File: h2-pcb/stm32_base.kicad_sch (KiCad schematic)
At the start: 42 parts, among them J1 Network Connector, J2 STDC14, SW1 SW_Push, U1 LD39050PU33R, U2 STM32G474RBT6, U3 SN65HVD230, Y1 8MHz

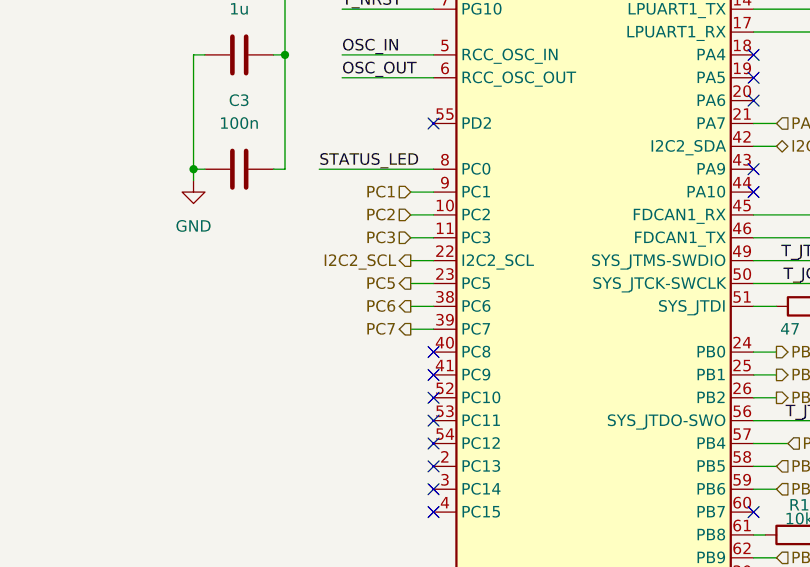
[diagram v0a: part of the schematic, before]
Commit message: Update sur le routage, silkscreen, jlcpcb parts #
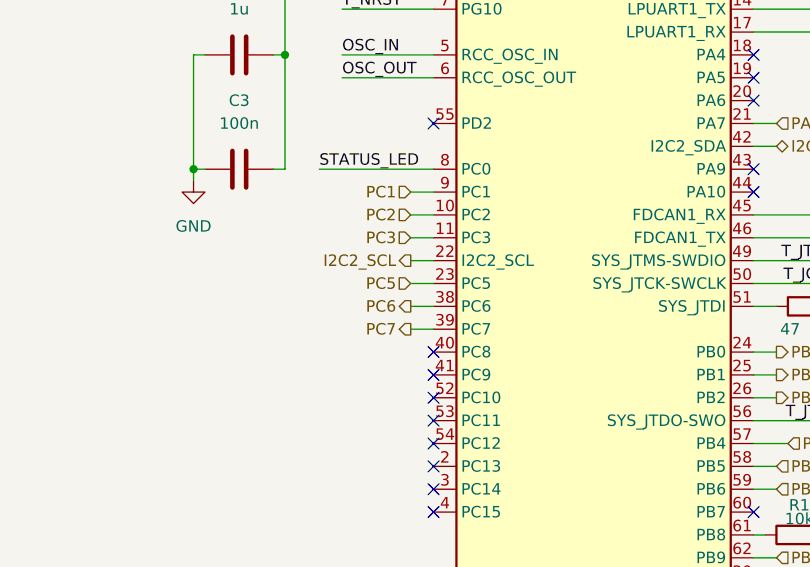
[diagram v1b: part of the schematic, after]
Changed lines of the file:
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@@
 	)
 	(hierarchical_label "PC5"
-		(shape output)
+		(shape input)
 		(at 60.96 130.81 180)
 		(effects

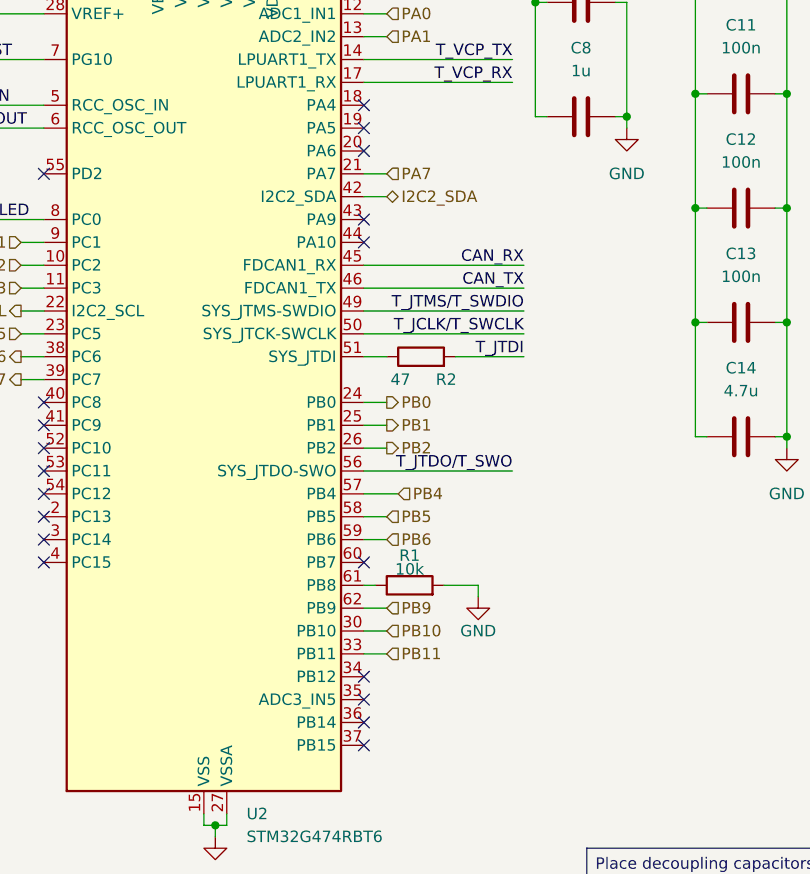
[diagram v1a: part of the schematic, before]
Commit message: h2-pcb: rename PA7 label to PB13
The pin function for PB13 on the MCU was modified, but the hierarchical
label wasn't updated. The one that used to be called "PA7" was renamed
to "PB13" and connected to that pin.

Also updated the routing to refelct these changes.
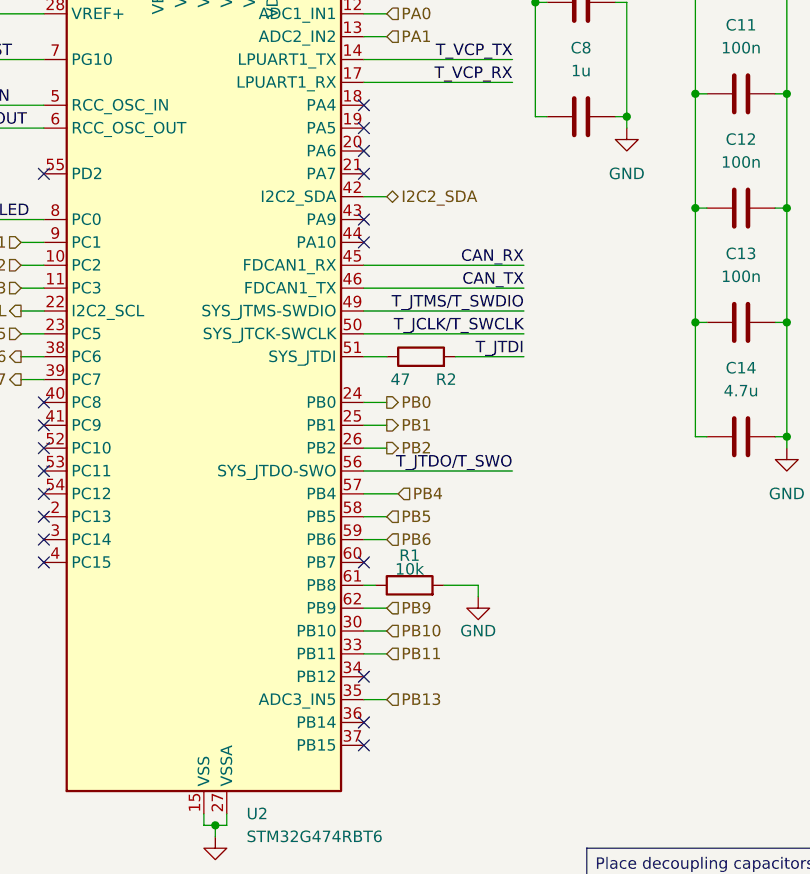
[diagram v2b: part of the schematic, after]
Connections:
- net PB13: now reaches U2.35 (PB13)
- net PA7: no longer names the net of U2.21 (PA7)
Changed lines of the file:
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@@
-	)
-	(no_connect
-		(at 99.06 171.45)
 	)
 	(no_connect
@@
 	)
 	(no_connect
+		(at 99.06 113.03)
+	)
+	(no_connect
 		(at 99.06 176.53)
 	)
@@
 	(wire
 		(pts
+			(xy 99.06 171.45) (xy 101.6 171.45)
+		)
+		(stroke
+			(width 0)
+			(type default)
+		)
+	)
+	(wire
+		(pts
 			(xy 144.78 104.14) (xy 146.05 104.14)
 		)
@@
 		(pts
 			(xy 135.89 116.84) (xy 135.89 129.54)
-		)
-		(stroke
-			(width 0)
-			(type default)
-		)
-	)
-	(wire
-		(pts
-			(xy 99.06 113.03) (xy 101.6 113.03)
 		)
 		(stroke
@@
 		)
 	)
-	(hierarchical_label "PA7"
-		(shape input)
-		(at 101.6 113.03 0)
-		(effects
-			(font
-				(size 1.27 1.27)
-			)
-			(justify left)
-		)
-	)
 	(hierarchical_label "PC7"
 		(shape output)
@@
 		(effects
 			(font
+				(size 1.27 1.27)
+			)
+			(justify left)
+		)
+	)
+	(hierarchical_label "PB13"
+		(shape input)
+		(at 101.6 171.45 0)
+		(effects
+			(font

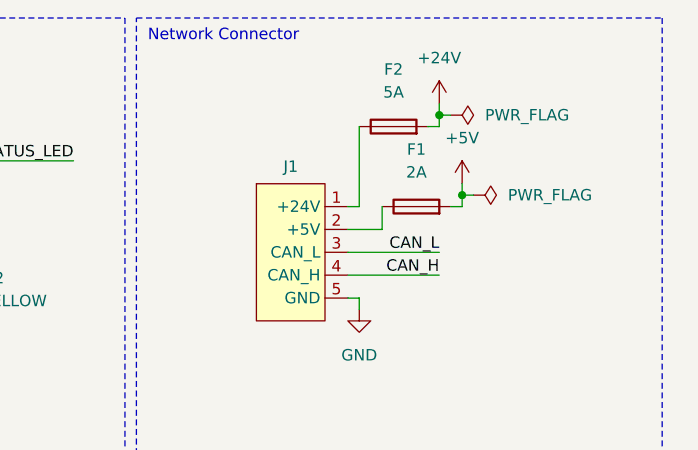
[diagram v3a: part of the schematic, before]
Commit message: h2-pcb: implement review comments
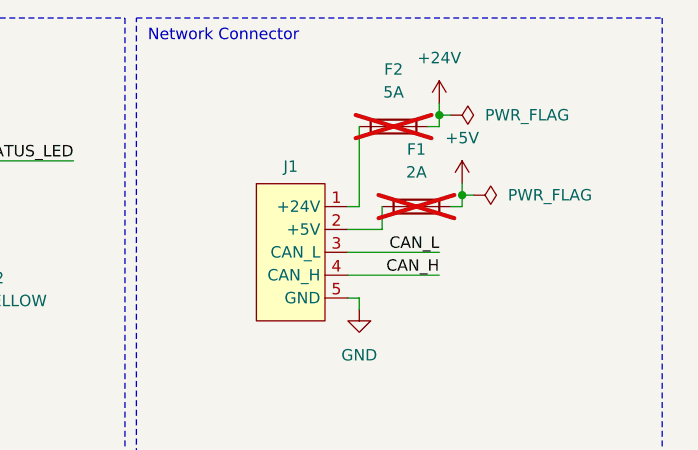
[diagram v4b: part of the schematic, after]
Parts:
- F1, F2: now not fitted
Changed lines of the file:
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@@
 		(in_bom yes)
 		(on_board yes)
-		(dnp no)
+		(dnp yes)
 		(fields_autoplaced yes)
 		(property "Reference" "F2"
@@
 		(in_bom yes)
 		(on_board yes)
-		(dnp no)
+		(dnp yes)
 		(fields_autoplaced yes)
 		(property "Reference" "F1"

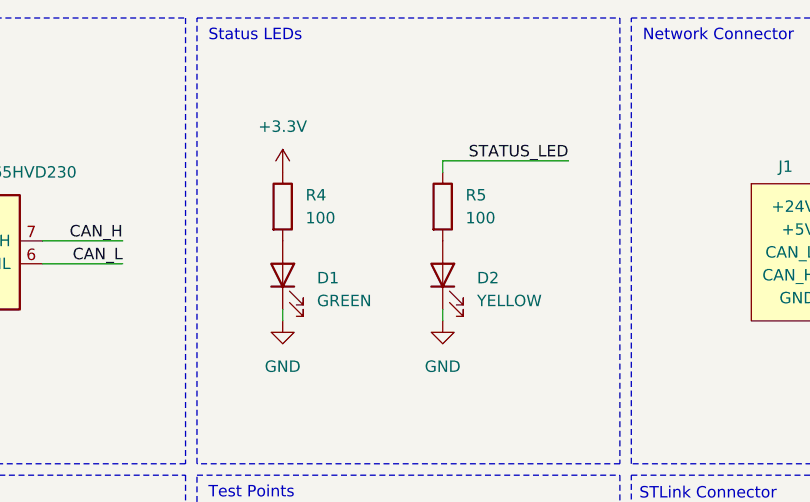
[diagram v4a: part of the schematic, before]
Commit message: h2-pcb: change value of LED resistors
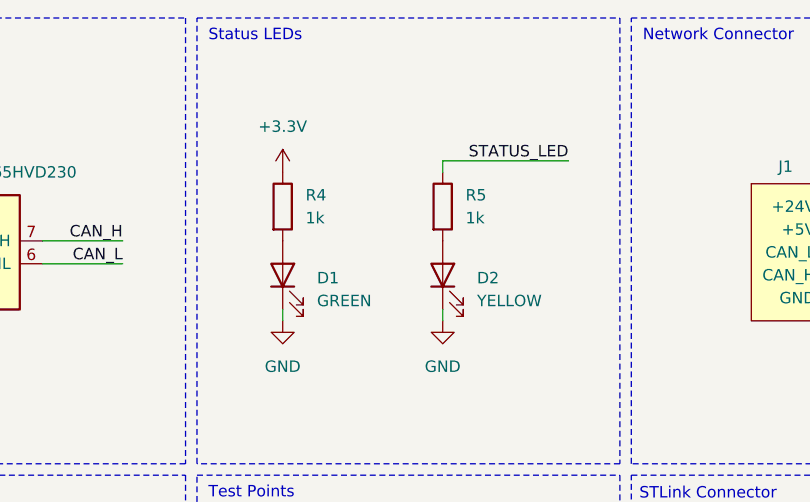
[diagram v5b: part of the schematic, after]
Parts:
- R4, R5: value 100 -> 1k; JLCPCB C25076 -> C11702
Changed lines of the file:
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@@
 			)
 		)
-		(property "Value" "100"
+		(property "Value" "1k"
 			(at 189.23 35.5599 0)
 			(effects
@@
 			)
 		)
-		(property "JLCPCB" "C25076"
+		(property "JLCPCB" "C11702"
 			(at 186.69 34.29 0)
 			(effects
@@
 			)
 		)
-		(property "Value" "100"
+		(property "Value" "1k"
 			(at 207.01 35.5599 0)
 			(effects
@@
 			)
 		)
-		(property "JLCPCB" "C25076"
+		(property "JLCPCB" "C11702"
 			(at 204.47 34.29 0)
 			(effects

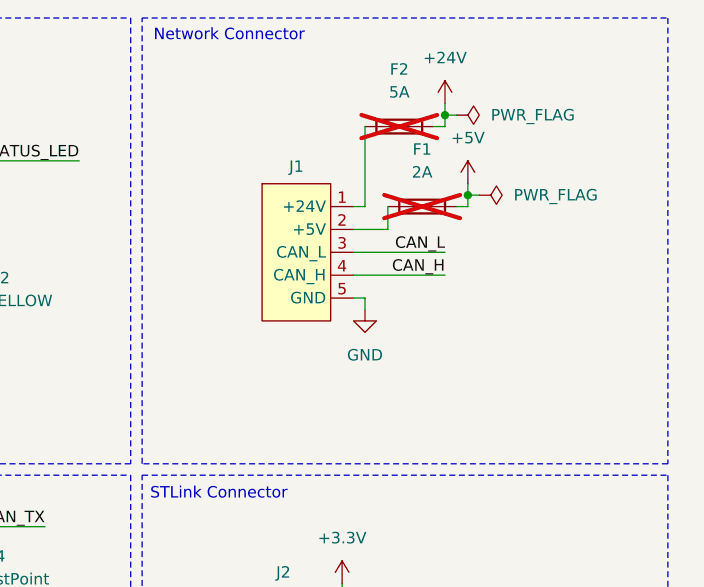
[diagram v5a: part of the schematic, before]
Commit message: h2-pcb: add fuse holder 01110501Z
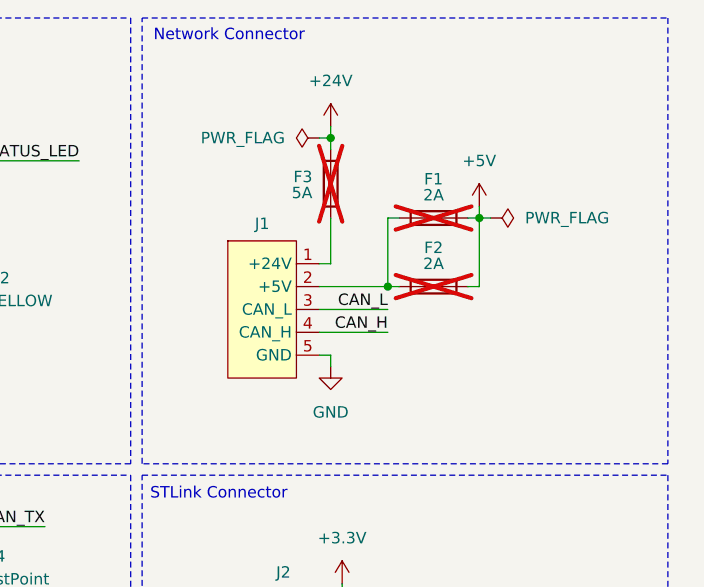
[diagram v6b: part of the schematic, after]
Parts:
- added F2: 2A, Fuse:Fuseholder_Clip-5x20mm_Littelfuse_111_Lateral_P18.80x5.00mm_D1.17mm_Horizontal, symbol Device:Fuse
- renumbered F2 to F3
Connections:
- net +5V: now also F2.2
- net at F1.1, J1.2 (+5V): now also F2.1
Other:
- moved on the sheet: F1, F3, J1

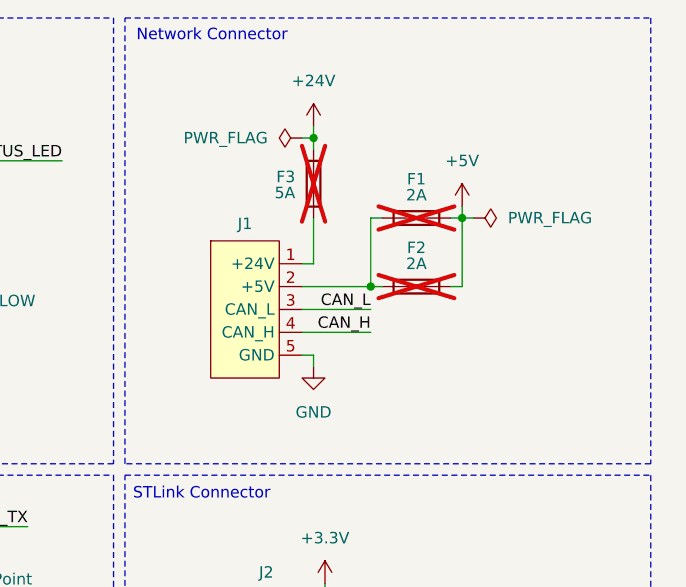
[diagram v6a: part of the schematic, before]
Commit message: h2-pcb: add fuse holder 01110501Z for 5A
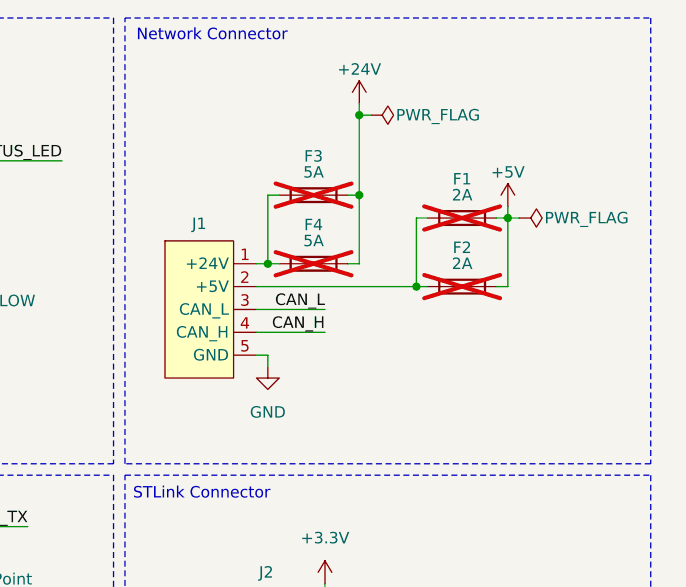
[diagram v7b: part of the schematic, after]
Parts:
- added F4: 5A, Fuse:Fuseholder_Clip-5x20mm_Littelfuse_111_Lateral_P18.80x5.00mm_D1.17mm_Horizontal, symbol Device:Fuse
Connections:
- net +24V: now also F4.2
- net at F3.1, J1.1 (+24V): now also F4.1
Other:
- moved on the sheet: F1, F2, F3, J1

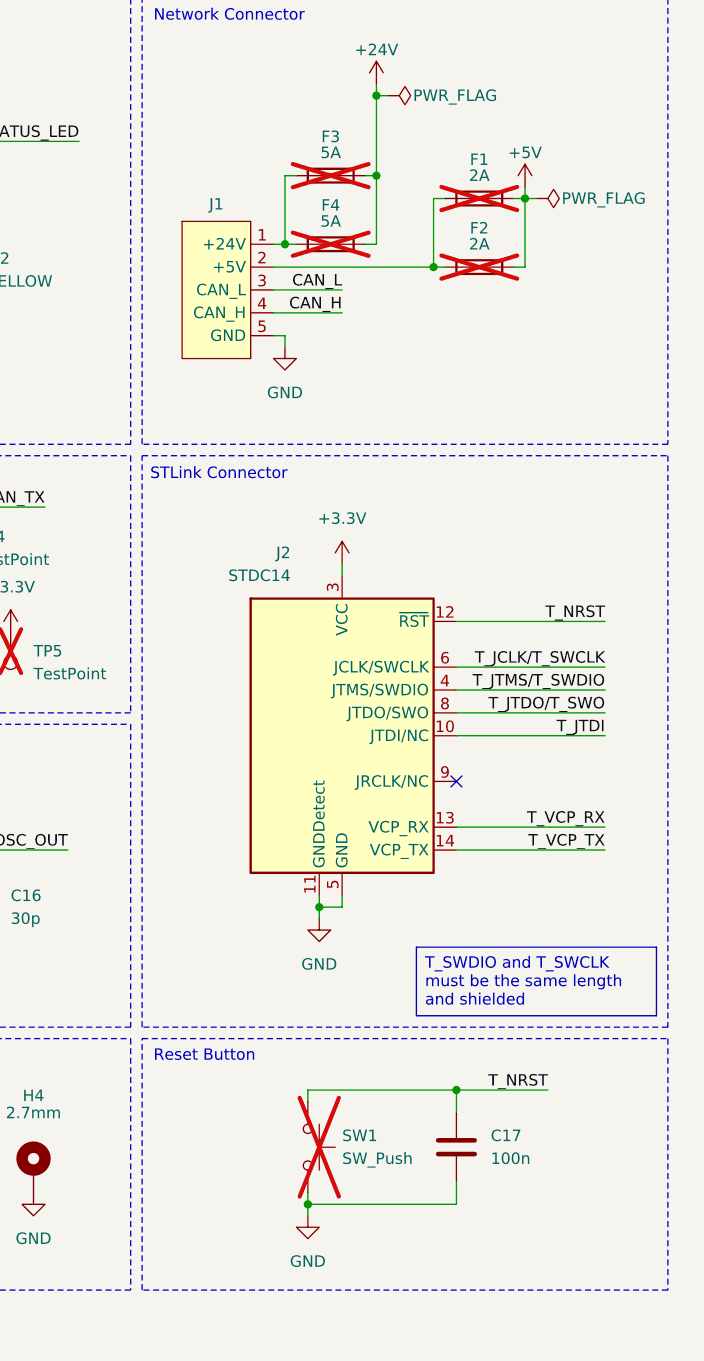
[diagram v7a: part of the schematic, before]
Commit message: h2-pcb: change MOSFET pins and part number
The orientation of the footprint did not match that of the actual
package. Also, the assembled parts have been changed.
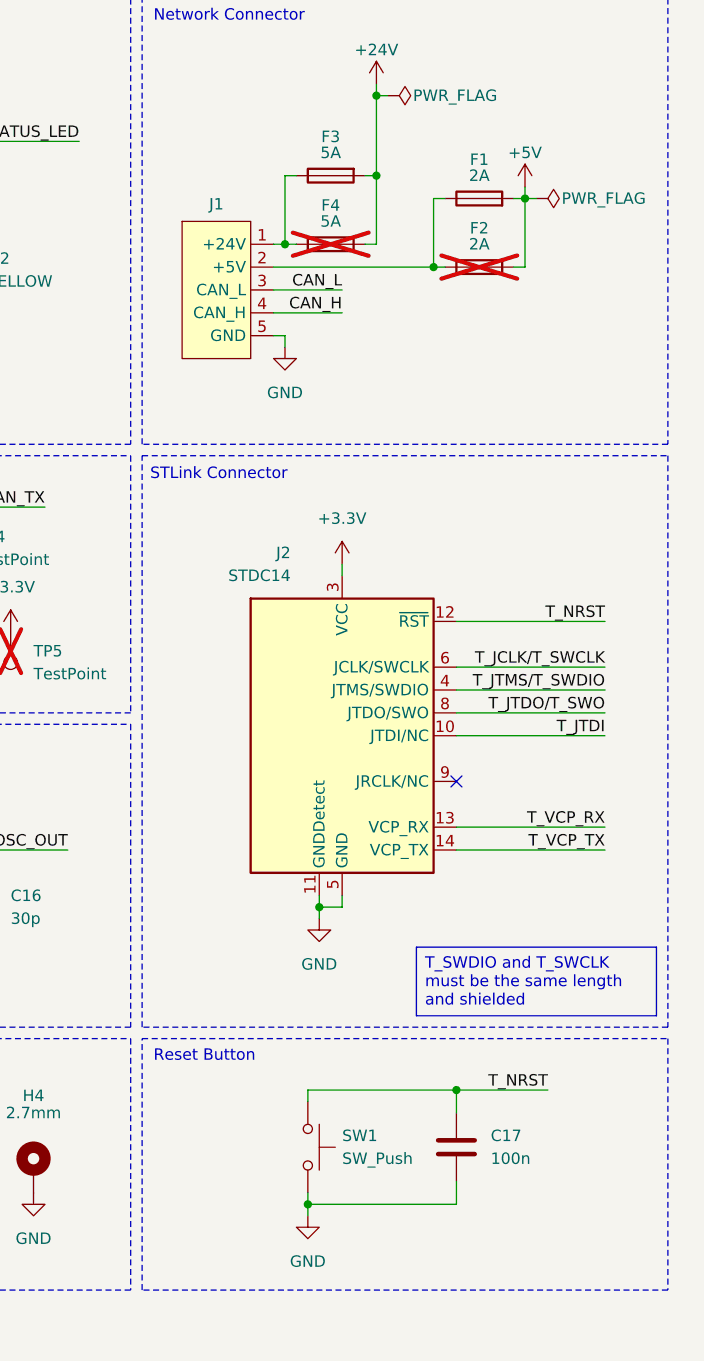
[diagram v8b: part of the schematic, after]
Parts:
- F1, F3, SW1: now fitted
